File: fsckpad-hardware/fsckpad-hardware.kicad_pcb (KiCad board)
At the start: 2 copper layers, 158.1 x 78.3 mm, 55 parts, among them IC1 LS20-S, IC3 ICM-42670-P, IC4 PCA9555D, IC5 PCA9555D, IC6 LS20-S, U1 DRV2605LDGS, X1 1-TS009, Y1 1-TS009

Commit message: work
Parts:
- LT1, RT1: moved to B.Cu
- moved LT1 2.82 mm to (34.8, 14.1), turned to 180 degrees
- moved RT1 2.60 mm to (145.8, 14.1), turned to 180 degrees
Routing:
- net +3.3V: track 478.2 -> 439.1 mm
- net GND: track 8.94 -> 16.1 mm, vias 46 -> 48
- net /LT: track 82.2 -> 84.6 mm
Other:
- board text added: "rev 1.1"
- board text removed: "rev 1.0H"

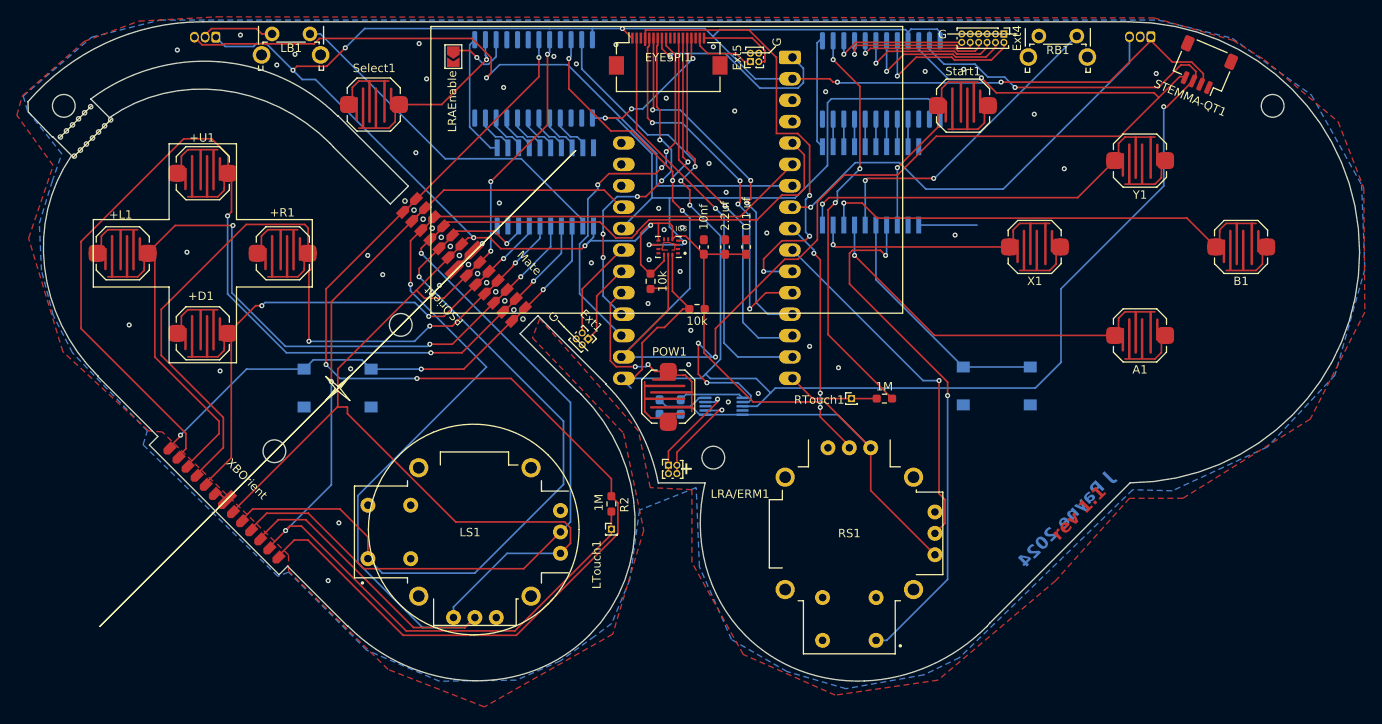
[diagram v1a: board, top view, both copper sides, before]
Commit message: starting enclosure, fixing board bugs
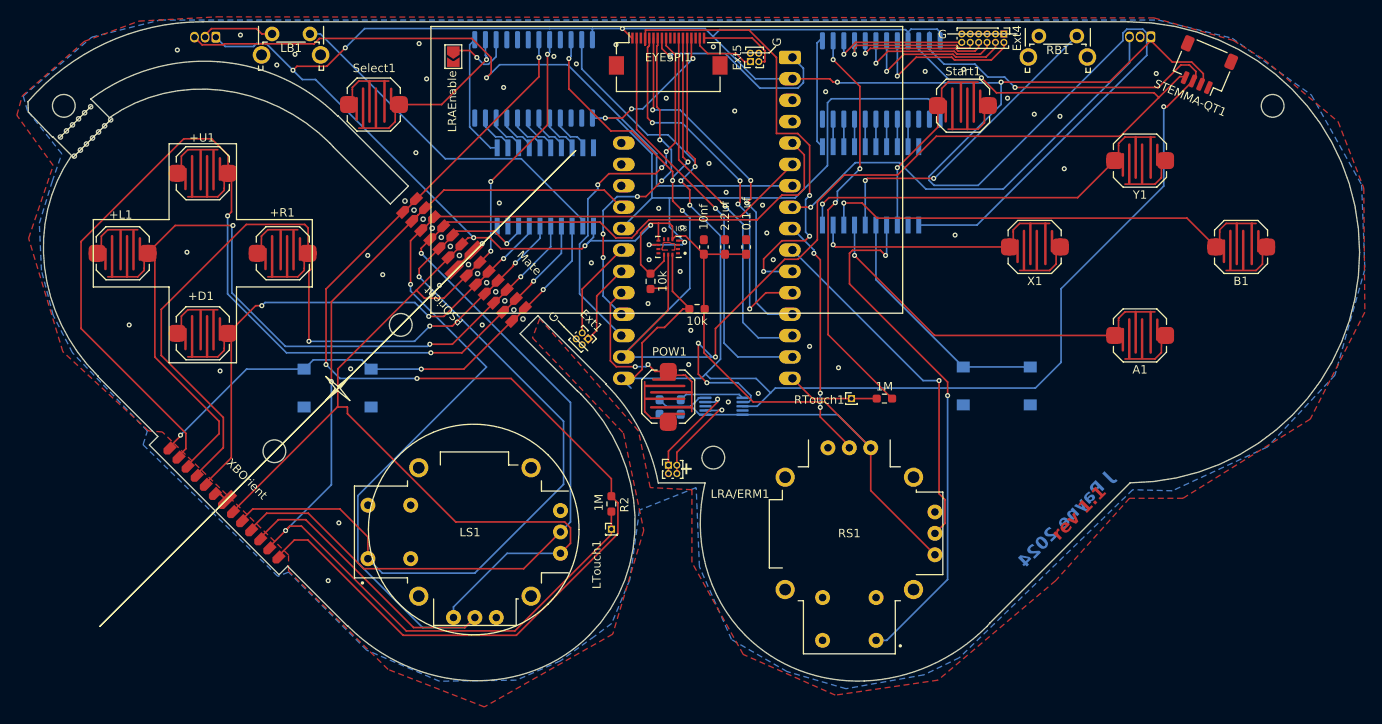
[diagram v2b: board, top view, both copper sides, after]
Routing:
- net +3.3V: track 439.1 -> 519.9 mm
- net GND: vias 48 -> 53
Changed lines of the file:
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@@
 		(at 34.990369 70.165631 45)
 		(property "Reference" "XBOrient"
-			(at 5.0263 -0.089803 315)
+			(at 5.0263 -0.089803 -45)
 			(unlocked yes)
 			(layer "F.SilkS")
@@
 		(tags "solder jumper open")
 		(property "Reference" "LRAEnable"
-			(at 5.3105 0.127 270)
+			(at 5.3105 0.127 -90)
 			(layer "F.SilkS")
 			(effects
@@
 		(at 64.252781 40.549965 45)
 		(property "Reference" "Mate"
-			(at 5.241206 5.727745 315)
+			(at 5.241206 5.727745 -45)
 			(unlocked yes)
 			(layer "F.SilkS")
@@
 		(tags "VSSOP SO")
 		(property "Reference" "U1"
-			(at 0 2.45 360)
+			(at 0 2.45 0)
 			(layer "B.SilkS")
 			(effects
@@
 		)
 		(property "Value" "DRV2605LDGS"
-			(at 0 -2.45 360)
+			(at 0 -2.45 0)
 			(layer "B.Fab")
 			(effects
@@
 		)
 		(fp_text user "${REFERENCE}"
-			(at 0 0 360)
+			(at 0 0 0)
 			(layer "B.Fab")
 			(effects
@@
 		(tags "tact sw push 6mm smd")
 		(property "Reference" "RPDL1"
-			(at 0 4.05 360)
+			(at 0 4.05 0)
 			(layer "B.SilkS")
 			(effects
@@
 		)
 		(property "Value" "1-TS009"
-			(at 0 -4.15 360)
+			(at 0 -4.15 0)
 			(layer "B.Fab")
 			(effects
@@
 		)
 		(fp_text user "${REFERENCE}"
-			(at 0 4.05 360)
+			(at 0 4.05 0)
 			(layer "B.Fab")
 			(effects
@@
 	)
 	(segment
+		(start 144.848175 13.1562)
+		(end 145.3038 13.611825)
+		(width 0.2)
+		(layer "B.Cu")
+		(net 1)
+	)
+	(segment
 		(start 43.953845 18.022155)
 		(end 45.057888 19.126199)
@@
 	)
 	(segment
+		(start 119.4622 30.632022)
+		(end 119.4622 31.089978)
+		(width 0.2)
+		(layer "B.Cu")
+		(net 1)
+	)
+	(segment
 		(start 117.3198 13.149201)
 		(end 116.967 13.502001)
@@
 	)
 	(segment
+		(start 145.3038 13.611825)
+		(end 145.3038 16.257926)
+		(width 0.2)
+		(layer "B.Cu")
+		(net 1)
+	)
+	(segment
 		(start 116.967 13.502001)
 		(end 116.666999 13.202)
@@
 	)
 	(segment
+		(start 145.3038 16.257926)
+		(end 125.161726 36.4)
+		(width 0.2)
+		(layer "B.Cu")
+		(net 1)
+	)
+	(segment
+		(start 128.016 19.431)
+		(end 128.016 22.078222)
+		(width 0.2)
+		(layer "B.Cu")
+		(net 1)
+	)
+	(segment
 		(start 116.666999 13.202)
 		(end 94.621 13.202)
@@
 	)
 	(segment
+		(start 142.933825 13.1562)
+		(end 144.848175 13.1562)
+		(width 0.2)
+		(layer "B.Cu")
+		(net 1)
+	)
+	(segment
 		(start 87.455684 57.157636)
 		(end 87.471684 57.141636)
@@
 	)
 	(segment
+		(start 128.016 22.078222)
+		(end 119.4622 30.632022)
+		(width 0.2)
+		(layer "B.Cu")
+		(net 1)
+	)
+	(segment
 		(start 79.502 13.075)
 		(end 74.422 13.075)
@@
 	)
 	(segment
+		(start 142.4782 14.506175)
+		(end 142.4782 13.611825)
+		(width 0.2)
+		(layer "B.Cu")
+		(net 1)
+	)
+	(segment
+		(start 120.060255 31.688033)
+		(end 125.296342 31.688033)
+		(width 0.2)
+		(layer "B.Cu")
+		(net 1)
+	)
+	(segment
 		(start 127.924 19.523)
 		(end 108.677 19.523)
@@
 	)
 	(segment
+		(start 142.4782 13.611825)
+		(end 142.933825 13.1562)
+		(width 0.2)
+		(layer "B.Cu")
+		(net 1)
+	)
+	(segment
 		(start 97.323 58.912)
 		(end 92.923 58.912)
@@
 	)
 	(segment
+		(start 125.296342 31.688033)
+		(end 142.4782 14.506175)
+		(width 0.2)
+		(layer "B.Cu")
+		(net 1)
+	)
+	(segment
 		(start 79.629 36.527)
 		(end 79.629 37.846)
@@
 	)
 	(segment
+		(start 119.4622 31.089978)
+		(end 120.060255 31.688033)
+		(width 0.2)
+		(layer "B.Cu")
+		(net 1)
+	)
+	(segment
 		(start 46.626707 19.126199)
 		(end 65.405 37.904492)
@@
 	)
 	(via
+		(at 66.421 48.26)
+		(size 0.6)
+		(drill 0.3)
+		(layers "F.Cu" "B.Cu")
+		(free yes)
+		(net 2)
+	)
+	(via
 		(at 68.961 20.066)
 		(size 0.6)
@@
 	)
 	(via
+		(at 100.965 40.513)
+		(size 0.6)
+		(drill 0.3)
+		(layers "F.Cu" "B.Cu")
+		(free yes)
+		(net 2)
+	)
+	(via
 		(at 49.403 71.755)
 		(size 0.6)
@@
 	)
 	(via
+		(at 99.695 34.036)
+		(size 0.6)
+		(drill 0.3)
+		(layers "F.Cu" "B.Cu")
+		(free yes)
+		(net 2)
+	)
+	(via
 		(at 99.187 56.388)
 		(size 0.6)
@@
 	)
 	(via
+		(at 135.001 23.495)
+		(size 0.6)
+		(drill 0.3)
+		(layers "F.Cu" "B.Cu")
+		(free yes)
+		(net 2)
+	)
+	(via
 		(at 44.196 16.129)
 		(size 0.6)
@@
 		(size 0.6)
 		(drill 0.3)
+		(layers "F.Cu" "B.Cu")
+		(free yes)
+		(net 2)
+	)
+	(via
+		(at 128.778 21.336)
+		(size 0.6)
+		(drill 0.3)

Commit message: rev 1
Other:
- outline, holes or cut-outs redrawn
